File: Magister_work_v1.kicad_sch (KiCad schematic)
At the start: 0 parts

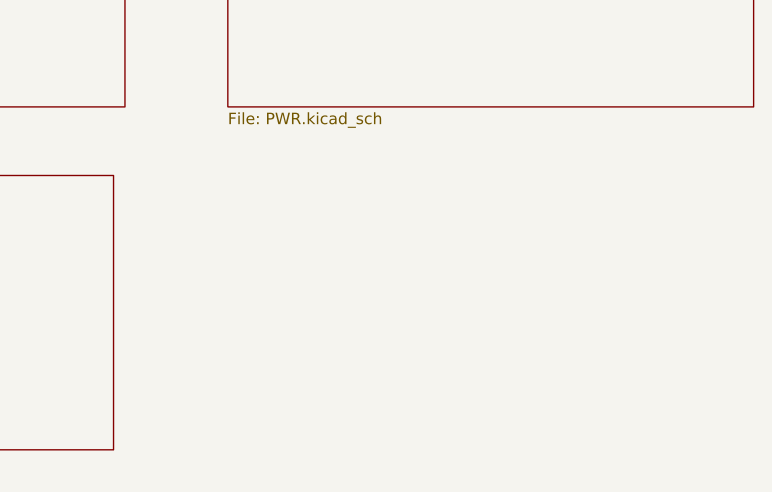
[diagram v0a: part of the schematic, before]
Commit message: feat: добавлен вход питания, кроме dc-dc
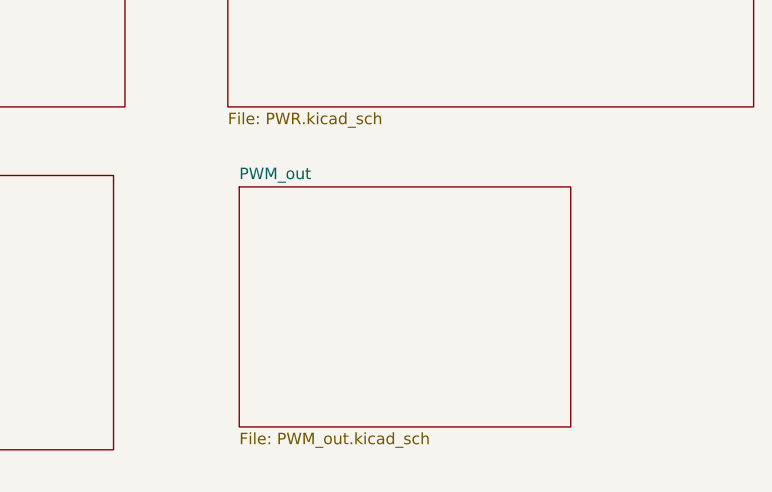
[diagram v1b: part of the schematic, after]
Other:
- added sheet PWM_out (PWM_out.kicad_sch)
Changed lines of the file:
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@@
+	)
+	(sheet
+		(at 105.41 74.93)
+		(size 36.83 26.67)
+		(exclude_from_sim no)
+		(in_bom yes)
+		(on_board yes)
+		(dnp no)
+		(fields_autoplaced yes)
+		(stroke
+			(width 0.1524)
+			(type solid)
+		)
+		(fill
+			(color 0 0 0 0)
+		)
+		(property "Sheetname" "PWM_out"
+			(at 105.41 74.2184 0)
+			(show_name no)
+			(do_not_autoplace no)
+			(effects
+				(font
+					(size 1.27 1.27)
+				)
+				(justify left bottom)
+			)
+		)
+		(property "Sheetfile" "PWM_out.kicad_sch"
+			(at 105.41 102.1846 0)
+			(show_name no)
+			(do_not_autoplace no)
+			(effects
+				(font
+					(size 1.27 1.27)
+				)
+				(justify left top)
+			)
+		)
+		(instances
+			(project "Magister_work_v1"
+				(path "/9ff4e5e8-ab59-4c4d-a10a-f8f5e444c5cb"
+					(page "5")
+				)
+			)
+		)
 	)
 	(sheet

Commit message: feat: Добавил внешние интерфейсы
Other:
- added sheet External_interfaces (External_interfaces.kicad_sch)
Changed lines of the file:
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@@
+	)
+	(sheet
+		(at 87.63 120.65)
+		(size 48.26 22.86)
+		(exclude_from_sim no)
+		(in_bom yes)
+		(on_board yes)
+		(dnp no)
+		(fields_autoplaced yes)
+		(stroke
+			(width 0.1524)
+			(type solid)
+		)
+		(fill
+			(color 0 0 0 0)
+		)
+		(property "Sheetname" "External_interfaces"
+			(at 87.63 119.9384 0)
+			(show_name no)
+			(do_not_autoplace no)
+			(effects
+				(font
+					(size 1.27 1.27)
+				)
+				(justify left bottom)
+			)
+		)
+		(property "Sheetfile" "External_interfaces.kicad_sch"
+			(at 87.63 144.0946 0)
+			(show_name no)
+			(do_not_autoplace no)
+			(effects
+				(font
+					(size 1.27 1.27)
+				)
+				(justify left top)
+			)
+		)
+		(instances
+			(project "Magister_work_v1"
+				(path "/9ff4e5e8-ab59-4c4d-a10a-f8f5e444c5cb"
+					(page "6")
+				)
+			)
+		)
 	)
 	(sheet
